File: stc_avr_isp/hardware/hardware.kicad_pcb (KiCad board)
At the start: 2 copper layers, 18 x 42.8 mm, 24 parts, among them J1 Conn_01x09_Socket, J2 Conn_01x09_Socket, J3 ISP, J4 TARGET VOLTAGE, J5 BAUD RATE, U1 74HC244, U2 AMS1117-3.3

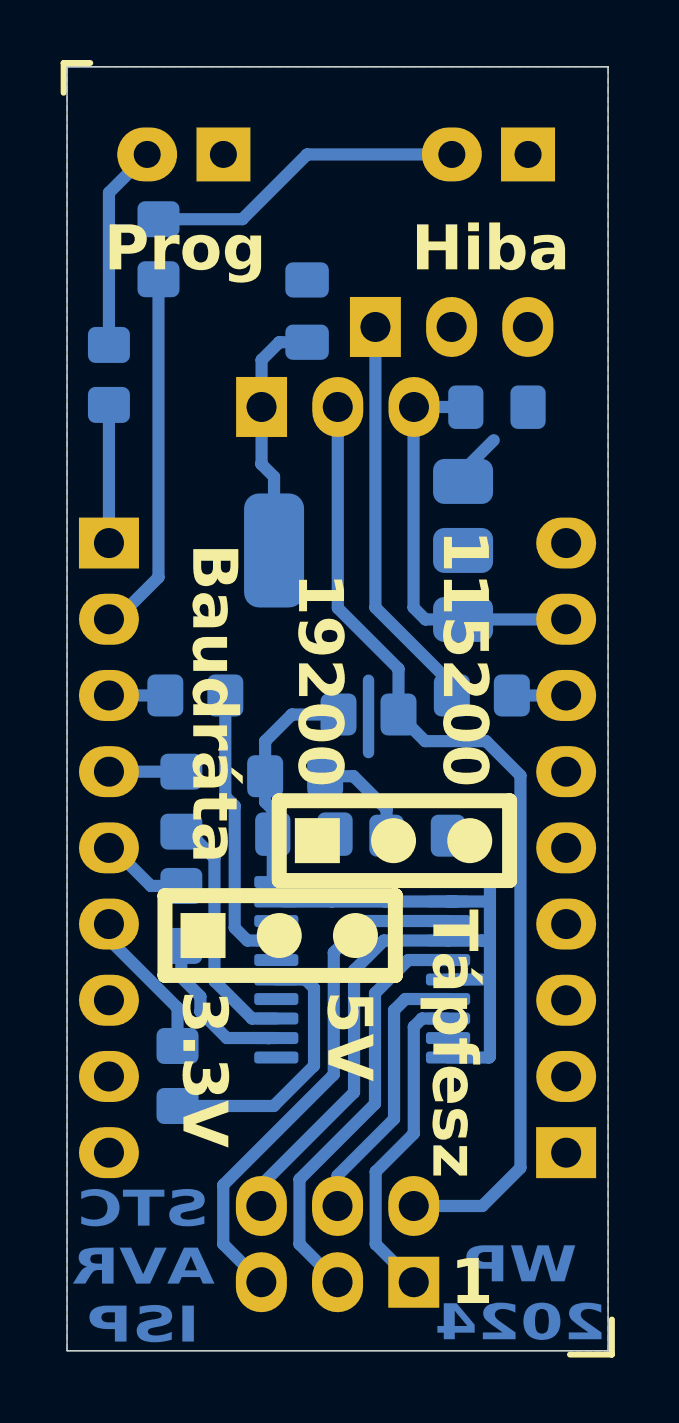
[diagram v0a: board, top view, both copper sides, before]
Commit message: Add fancy blink animation on reset, specify resistor values
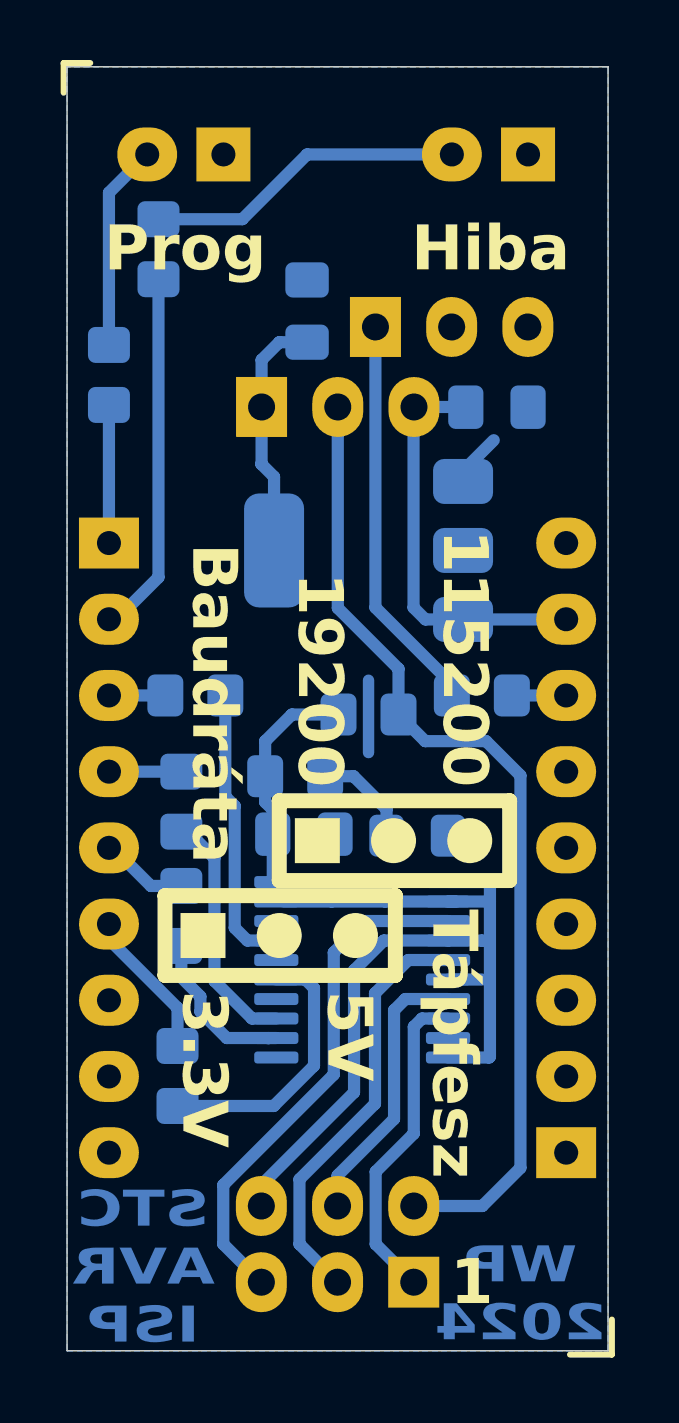
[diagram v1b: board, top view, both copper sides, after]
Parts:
- C2: value 100n -> 10u
- D1: value LED_Filled -> POWER
- R5, R7: value 330 -> 1k5
- R6: value 330 -> 1k
- R9: value 330 -> 270
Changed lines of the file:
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@@
 		(allow_soldermask_bridges_in_footprints no)
 		(pcbplotparams
-			(layerselection 0x00010fc_ffffffff)
-			(plot_on_all_layers_selection 0x0000000_00000000)
+			(layerselection 0x0000020_fffffffe)
+			(plot_on_all_layers_selection 0x0001000_00000000)
 			(disableapertmacros no)
 			(usegerberextensions no)
@@
 			(sketchpadsonfab no)
 			(subtractmaskfromsilk no)
-			(outputformat 1)
+			(outputformat 4)
 			(mirror no)
-			(drillshape 1)
+			(drillshape 2)
 			(scaleselection 1)
-			(outputdirectory "")
+			(outputdirectory "./")
 		)
 	)
@@
 			(at 0 0 90)
 			(size 2 1.7)
-			(drill 1)
+			(drill 0.9)
 			(layers "*.Cu" "*.Mask")
 			(remove_unused_layers no)
@@
 			(at 0 2.54 90)
 			(size 2 1.7)
-			(drill 1)
+			(drill 0.9)
 			(layers "*.Cu" "*.Mask")
 			(remove_unused_layers no)
@@
 			(at 0 5.08 90)
 			(size 2 1.7)
-			(drill 1)
+			(drill 0.9)
 			(layers "*.Cu" "*.Mask")
 			(remove_unused_layers no)
@@
 			(at 0 0 180)
 			(size 1.8 1.8)
-			(drill 0.9)
+			(drill 0.8)
 			(layers "*.Cu" "*.Mask")
 			(remove_unused_layers no)
@@
 			(at 2.54 0 180)
 			(size 2 1.8)
-			(drill 0.9)
+			(drill 0.8)
 			(layers "*.Cu" "*.Mask")
 			(remove_unused_layers no)
@@
 			(at 0 0 180)
 			(size 1.8 1.8)
-			(drill 0.9)
+			(drill 0.8)
 			(layers "*.Cu" "*.Mask")
 			(remove_unused_layers no)
@@
 			(at 2.54 0 180)
 			(size 2 1.8)
-			(drill 0.9)
+			(drill 0.8)
 			(layers "*.Cu" "*.Mask")
 			(remove_unused_layers no)
@@
 			(at 0 0 90)
 			(size 2 1.7)
-			(drill 1)
+			(drill 0.9)
 			(layers "*.Cu" "*.Mask")
 			(remove_unused_layers no)
@@
 			(at -2.54 0 90)
 			(size 2 1.7)
-			(drill 1)
+			(drill 0.9)
 			(layers "*.Cu" "*.Mask")
 			(remove_unused_layers no)
@@
 			(at 0 2.54 90)
 			(size 2 1.7)
-			(drill 1)
+			(drill 0.9)
 			(layers "*.Cu" "*.Mask")
 			(remove_unused_layers no)
@@
 			(at -2.54 2.54 90)
 			(size 2 1.7)
-			(drill 1)
+			(drill 0.9)
 			(layers "*.Cu" "*.Mask")
 			(remove_unused_layers no)
@@
 			(at 0 5.08 90)
 			(size 2 1.7)
-			(drill 1)
+			(drill 0.9)
 			(layers "*.Cu" "*.Mask")
 			(remove_unused_layers no)
@@
 			(at -2.54 5.08 90)
 			(size 1.7 1.7)
-			(drill 1)
+			(drill 0.9)
 			(layers "*.Cu" "*.Mask")
 			(remove_unused_layers no)
@@
 			(at 0 0 180)
 			(size 2 1.7)
-			(drill 1)
+			(drill 0.8)
 			(layers "*.Cu" "*.Mask")
 			(remove_unused_layers no)
@@
 			(at 0 2.54 180)
 			(size 2 1.7)
-			(drill 1)
+			(drill 0.8)
 			(layers "*.Cu" "*.Mask")
 			(remove_unused_layers no)
@@
 			(at 0 5.08 180)
 			(size 2 1.7)
-			(drill 1)
+			(drill 0.8)
 			(layers "*.Cu" "*.Mask")
 			(remove_unused_layers no)
@@
 			(at 0 7.62 180)
 			(size 2 1.7)
-			(drill 1)
+			(drill 0.8)
 			(layers "*.Cu" "*.Mask")
 			(remove_unused_layers no)
@@
 			(at 0 10.16 180)
 			(size 2 1.7)
-			(drill 1)
+			(drill 0.8)
 			(layers "*.Cu" "*.Mask")
 			(remove_unused_layers no)
@@
 			(at 0 12.7 180)
 			(size 2 1.7)
-			(drill 1)
+			(drill 0.8)
 			(layers "*.Cu" "*.Mask")
 			(remove_unused_layers no)
@@
 			(at 0 15.24 180)
 			(size 2 1.7)
-			(drill 1)
+			(drill 0.8)
 			(layers "*.Cu" "*.Mask")
 			(remove_unused_layers no)
@@
 			(at 0 17.78 180)
 			(size 2 1.7)
-			(drill 1)
+			(drill 0.8)
 			(layers "*.Cu" "*.Mask")
 			(remove_unused_layers no)
@@
 			(at 0 20.32 180)
 			(size 2 1.7)
-			(drill 1)
+			(drill 0.8)
 			(layers "*.Cu" "*.Mask")
 			(remove_unused_layers no)
@@
 			(at 0 0)
 			(size 2 1.7)
-			(drill 1)
+			(drill 0.8)
 			(layers "*.Cu" "*.Mask")
 			(remove_unused_layers no)
@@
 			(at 0 2.54)
 			(size 2 1.7)
-			(drill 1)
+			(drill 0.8)
 			(layers "*.Cu" "*.Mask")
 			(remove_unused_layers no)
@@
 			(at 0 5.08)
 			(size 2 1.7)
-			(drill 1)
+			(drill 0.8)
 			(layers "*.Cu" "*.Mask")
 			(remove_unused_layers no)
@@
 			(at 0 7.62)
 			(size 2 1.7)
-			(drill 1)
+			(drill 0.8)
 			(layers "*.Cu" "*.Mask")
 			(remove_unused_layers no)
@@
 			(at 0 10.16)
 			(size 2 1.7)
-			(drill 1)
+			(drill 0.8)
 			(layers "*.Cu" "*.Mask")
 			(remove_unused_layers no)
@@
 			(at 0 12.7)
 			(size 2 1.7)
-			(drill 1)
+			(drill 0.8)
 			(layers "*.Cu" "*.Mask")
 			(remove_unused_layers no)
@@
 			(at 0 15.24)
 			(size 2 1.7)
-			(drill 1)
+			(drill 0.8)
 			(layers "*.Cu" "*.Mask")
 			(remove_unused_layers no)
@@
 			(at 0 17.78)
 			(size 2 1.7)
-			(drill 1)
+			(drill 0.8)
 			(layers "*.Cu" "*.Mask")
 			(remove_unused_layers no)
@@
 			(at 0 20.32)
 			(size 2 1.7)
-			(drill 1)
+			(drill 0.8)
 			(layers "*.Cu" "*.Mask")
 			(remove_unused_layers no)
@@
 			(at 0 0 90)
 			(size 2 1.7)
-			(drill 1)
+			(drill 0.9)
 			(layers "*.Cu" "*.Mask")
 			(remove_unused_layers no)
@@
 			(at 0 2.54 90)
 			(size 2 1.7)
-			(drill 1)
+			(drill 0.9)
 			(layers "*.Cu" "*.Mask")
 			(remove_unused_layers no)
@@
 			(at 0 5.08 90)
 			(size 2 1.7)
-			(drill 1)
+			(drill 0.9)
 			(layers "*.Cu" "*.Mask")
 			(remove_unused_layers no)
@@
 			)
 		)
-		(property "Value" "330"
+		(property "Value" "1k5"
 			(at 0 -1.65 0)
 			(layer "B.Fab")
@@
 			)
 		)
-		(property "Value" "LED_Filled"
+		(property "Value" "POWER"
 			(at 0 -1.65 180)
 			(layer "B.Fab")
@@
 			)
 		)
-		(property "Value" "100n"
+		(property "Value" "10u"
 			(at 0 -1.68 0)
 			(layer "B.Fab")
@@
 		(tags "resistor handsolder")
 		(property "Reference" "R9"
-			(at 0 1.65 360)
+			(at 0 1.65 0)
 			(layer "B.SilkS")
 			(effects
@@
 			)
 		)
-		(property "Value" "330"
-			(at 0 -1.65 360)
+		(property "Value" "270"
+			(at 0 -1.65 0)
 			(layer "B.Fab")
 			(effects
@@
 		)
 		(fp_text user "${REFERENCE}"
-			(at 0 0 360)
+			(at 0 0 0)
 			(layer "B.Fab")
 			(effects
@@
 			)
 		)
-		(property "Value" "330"
+		(property "Value" "1k5"
 			(at 0 -1.65 -90)
 			(layer "B.Fab")
@@
 			)
 		)
-		(property "Value" "330"
+		(property "Value" "1k"
 			(at 0 -1.65 -90)
 			(layer "B.Fab")
